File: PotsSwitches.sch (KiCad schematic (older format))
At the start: 14 parts, among them U301 MCP4251, U302 TLP2361, U303 TLP2361, U304 TLP2361, U305 TLP2361, U306 TLP290-4

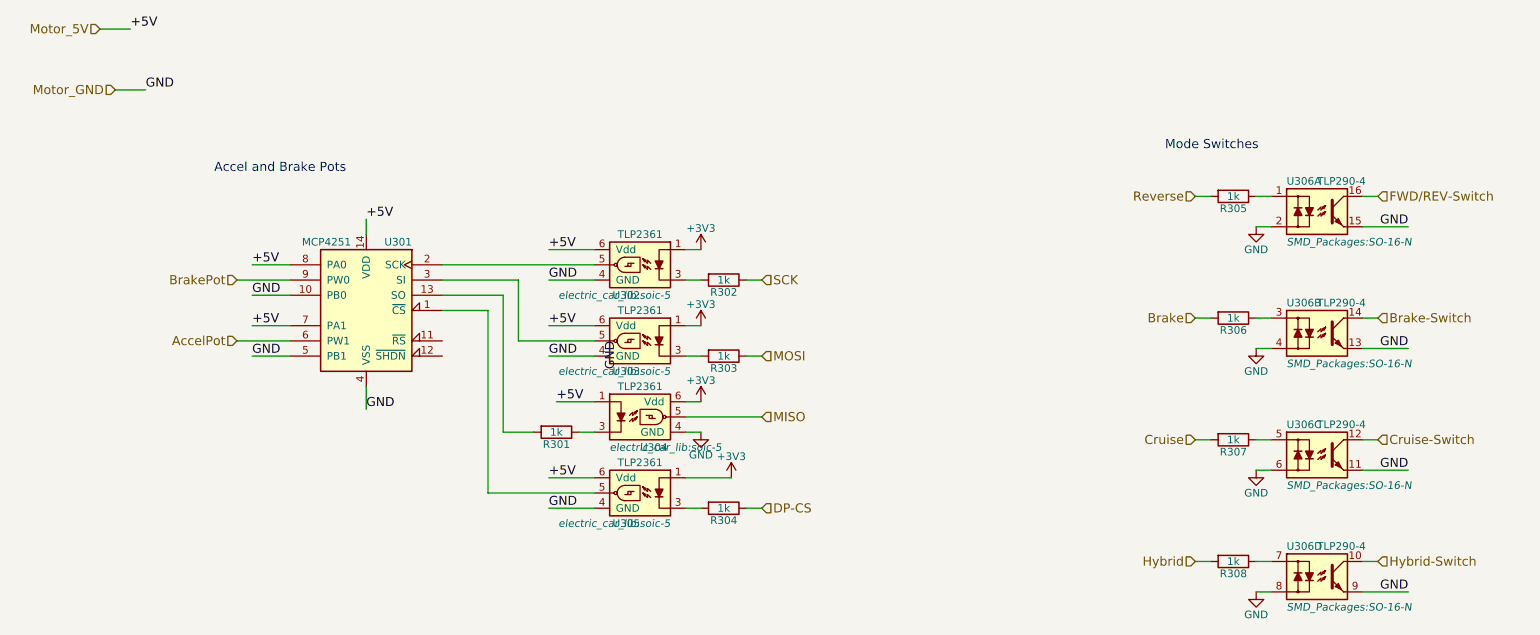
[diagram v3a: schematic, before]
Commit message: swapped pins, arranged parts
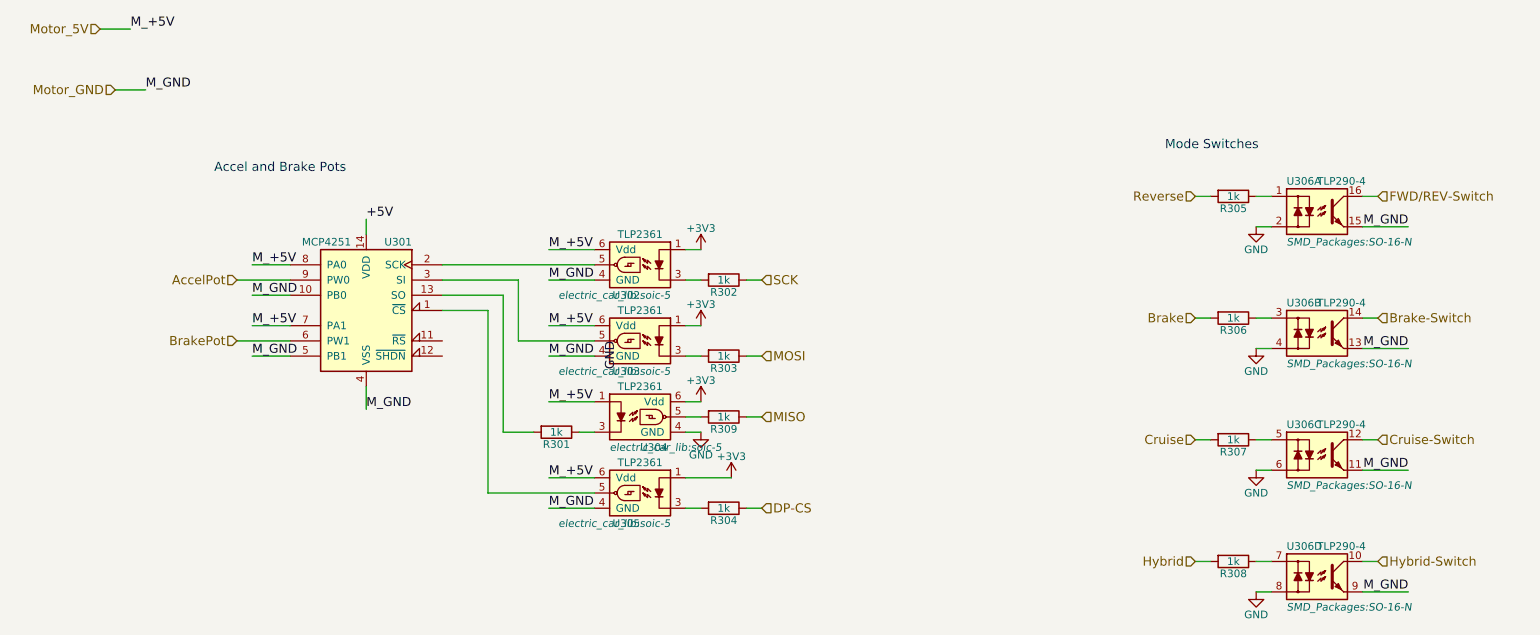
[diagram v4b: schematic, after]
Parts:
- added R309: 1k, Resistors_SMD:R_1206_HandSoldering, symbol R
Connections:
- net AccelPot: now also U301.9 (PW0); no longer U301.6 (PW1)
- net BrakePot: now also U301.6 (PW1); no longer U301.9 (PW0)
- net GND: no longer U301.10 (PB0), U301.4 (VSS), U301.5 (PB1), U302.4 (GND), U303.4 (GND), U305.4 (GND), U306.11, U306.13, U306.15, U306.9
- net MISO: now also R309.1; no longer U304.5
- net Motor_5V: no longer U301.14 (VDD)
- new net: R309.2, U304.5
- new net +5V: U301.14 (VDD)
- new net Motor_GND: U301.10 (PB0), U301.4 (VSS), U301.5 (PB1), U302.4 (GND), U303.4 (GND), U305.4 (GND), U306.11, U306.13, U306.15, U306.9
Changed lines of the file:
@@
 Wire Wire Line
 	2000 2650 2250 2650
-Text Label 2000 2650 0    60   ~ 0
-+5V
 Text Label 1300 1100 0    59   ~ 0
-GND
+M_GND
 Text Label 1200 700  0    60   ~ 0
-+5V
-Text Label 2000 2250 0    60   ~ 0
-+5V
+M_+5V
 Wire Wire Line
 	2000 2250 2250 2250
@@
 	1    0    0    -1
 $EndComp
-Text Label 3950 2150 0    60   ~ 0
-+5V
 Text Label 4400 2750 3    59   ~ 0
 GND
 Text Label 3950 2350 0    59   ~ 0
-GND
+M_GND
 Text Label 3950 2850 0    59   ~ 0
-GND
+M_GND
 $Comp
 L R R302
@@
 Wire Wire Line
 	3950 2150 4250 2150
-Text Label 3950 2650 0    60   ~ 0
-+5V
 Text Label 3950 3850 0    59   ~ 0
-GND
-Text Label 3950 3650 0    60   ~ 0
-+5V
+M_GND
 Wire Wire Line
 	5350 3850 5250 3850
@@
 	4950 3150 4850 3150
 Wire Wire Line
-	4850 3250 5350 3250
-Wire Wire Line
 	4850 3350 4950 3350
 Wire Wire Line
@@
 Wire Wire Line
 	3550 2550 3250 2550
-Text Label 4000 3150 0    60   ~ 0
-+5V
-Wire Wire Line
-	4000 3150 4250 3150
-Text Label 2750 3200 0    59   ~ 0
-GND
+Wire Wire Line
+	3950 3150 4250 3150
 Wire Wire Line
 	2750 3200 2750 3050
@@
 	1    0    0    -1
 $EndComp
-Text Label 9600 2000 2    59   ~ 0
-GND
 Wire Wire Line
 	9600 2000 9300 2000
-Text Label 9600 2800 2    59   ~ 0
-GND
-Text Label 9600 3600 2    59   ~ 0
-GND
-Text Label 9600 4400 2    59   ~ 0
-GND
 Wire Wire Line
 	9600 2800 9300 2800
@@
 Text HLabel 5350 3850 2    60   Input ~ 0
 DP-CS
+Text HLabel 1900 2750 0    60   Input ~ 0
+BrakePot
 Text HLabel 1900 2350 0    60   Input ~ 0
-BrakePot
-Text HLabel 1900 2750 0    60   Input ~ 0
 AccelPot
 Wire Wire Line
@@
 Wire Wire Line
 	2250 2750 1900 2750
-Text Label 2000 2450 0    59   ~ 0
-GND
 Wire Wire Line
 	2000 2450 2250 2450
-Text Label 2000 2850 0    59   ~ 0
-GND
 Wire Wire Line
 	2000 2850 2250 2850
@@
 	-1   0    0    -1
 $EndComp
+$Comp
+L R R309
+U 1 1 582C64A8
+P 5100 3250
+F 0 "R309" V 5180 3250 50  0000 C CNN
+F 1 "1k" V 5100 3250 50  0000 C CNN
+F 2 "Resistors_SMD:R_1206_HandSoldering" V 5030 3250 50  0001 C CNN
+F 3 "" H 5100 3250 50  0000 C CNN
+	1    5100 3250
+	0    1    1    0
+$EndComp
+Wire Wire Line
+	5350 3250 5250 3250
+Wire Wire Line
+	4950 3250 4850 3250
+Text Label 2000 2250 0    60   ~ 0
+M_+5V
+Text Label 2000 2650 0    60   ~ 0
+M_+5V
+Text Label 2000 2450 0    59   ~ 0
+M_GND
+Text Label 2000 2850 0    59   ~ 0
+M_GND
+Text Label 3950 2150 0    60   ~ 0
+M_+5V
+Text Label 3950 3150 0    60   ~ 0
+M_+5V
+Text Label 3950 2650 0    60   ~ 0
+M_+5V
+Text Label 3950 3650 0    60   ~ 0
+M_+5V
+Text Label 9600 2000 2    59   ~ 0
+M_GND
+Text Label 9600 2800 2    59   ~ 0
+M_GND
+Text Label 9600 3600 2    59   ~ 0
+M_GND
+Text Label 9600 4400 2    59   ~ 0
+M_GND
+Text Label 2750 3200 0    59   ~ 0
+M_GND
 $EndSCHEMATC

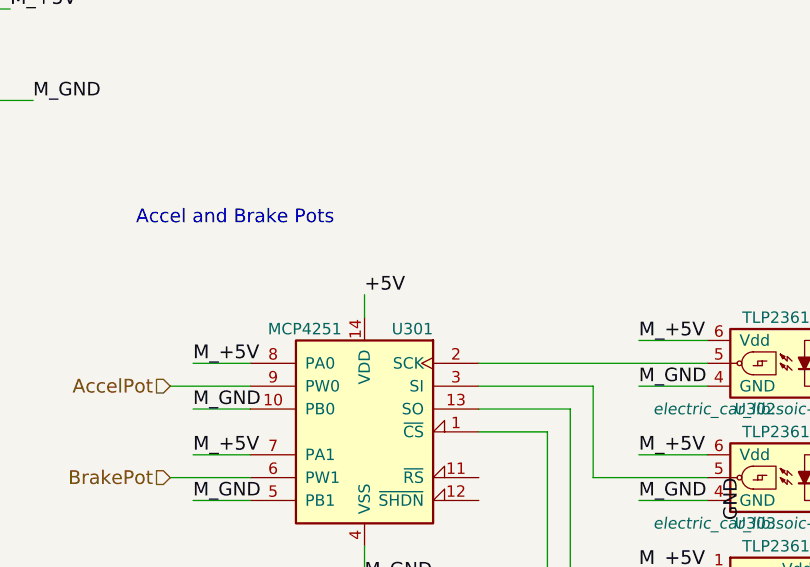
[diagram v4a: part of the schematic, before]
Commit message: laid out halls and pots
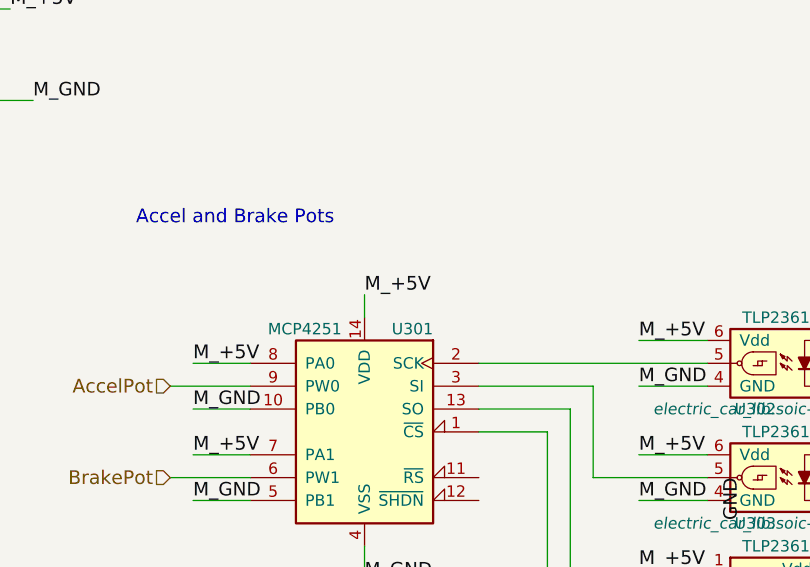
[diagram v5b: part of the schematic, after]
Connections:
- net +5V is gone; now on net Motor_5V: U301.14 (VDD)
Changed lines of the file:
@@
 Wire Wire Line
 	2750 3200 2750 3050
-Text Label 2750 1950 0    60   ~ 0
-+5V
 Wire Wire Line
 	2750 1950 2750 2050
@@
 Text Label 2750 3200 0    59   ~ 0
 M_GND
+Text Label 2750 1950 0    60   ~ 0
+M_+5V
 $EndSCHEMATC
